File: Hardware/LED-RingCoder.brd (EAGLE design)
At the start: 40.6 x 40.6 mm, 37 parts, among them IC1 74LS595D, IC2 74LS595D, U1 ENCODER_RGB

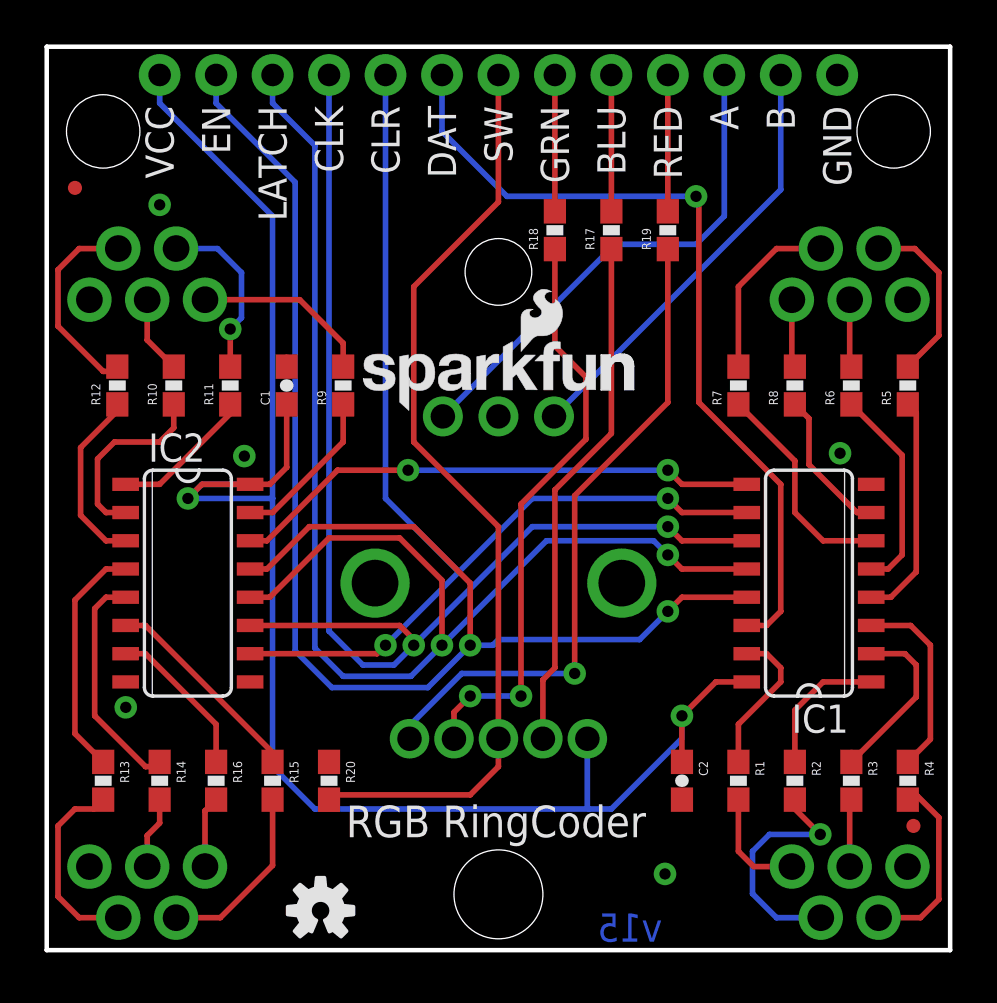
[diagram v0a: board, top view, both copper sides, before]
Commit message: Adding EN/GND and CLR/VCC jumpers
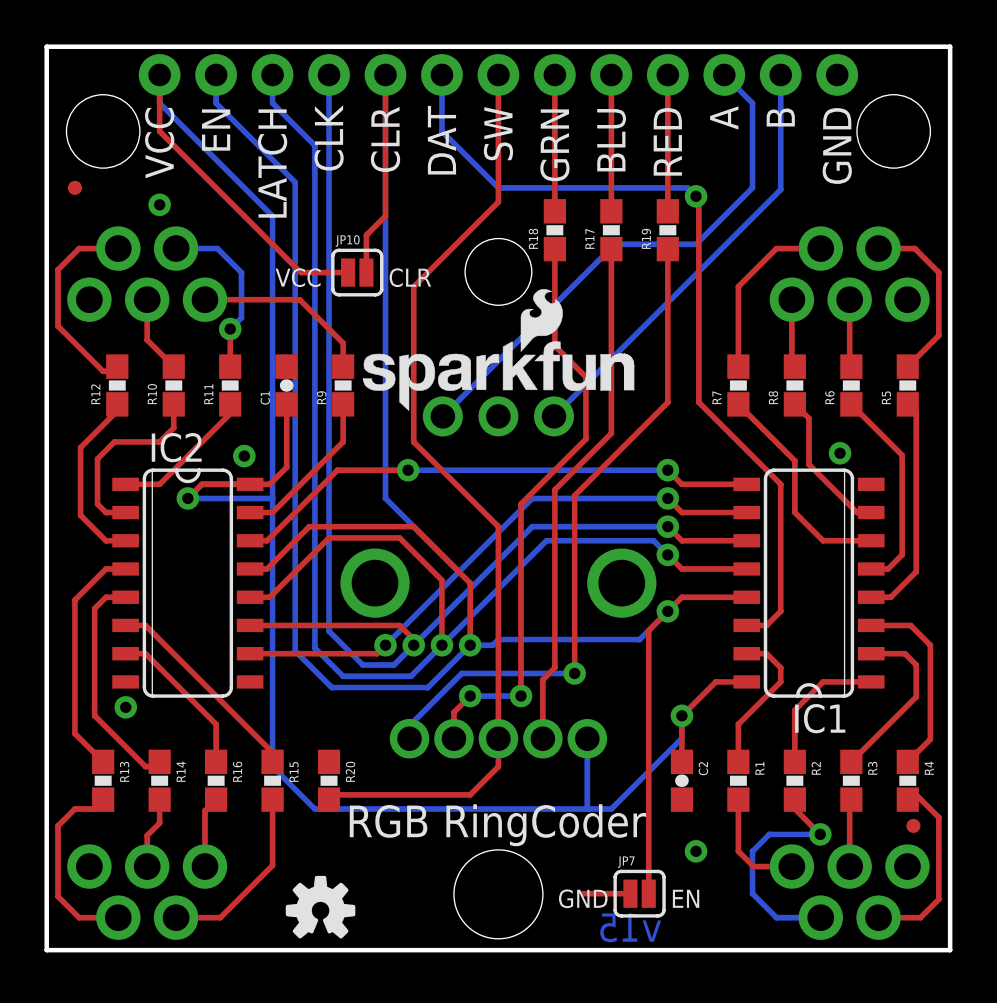
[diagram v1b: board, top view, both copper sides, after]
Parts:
- added JP10, JP7: (no value), SparkFun-Passives:SJ_2S
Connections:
- net CLEAR: now also JP10.2
- net EN: now also JP7.2
- net GND: now also JP7.1
- net VCC: now also JP10.1
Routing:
- net VCC: track 78.3 -> 91.9 mm
- net EN: track 64.6 -> 77.7 mm
- net CLEAR: track 49.2 -> 58.5 mm
- net GND: track 0.42 -> 2.55 mm
- net A: track 22.7 -> 23.8 mm

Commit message: Moving VCC/CLR jumper
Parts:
- moved JP10 27.9 mm to (14.0, 2.54), turned to 180 degrees
- moved U$2 19.0 mm to (31.4, 1.78)
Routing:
- net VCC: track 91.9 -> 84.1 mm, vias 2 -> 3
- net CLEAR: track 58.5 -> 60.9 mm, vias 2 -> 4
- net GND: vias 5 -> 6
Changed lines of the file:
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@@
 <text x="27.305" y="-10.16" size="1.778" layer="51" font="vector" ratio="15">Jim Lindblom</text>
 <text x="27.305" y="-13.335" size="1.778" layer="51" font="vector" ratio="15">Toni Klopfenstein</text>
-<text x="10.287" y="29.845" size="0.8128" layer="21" font="vector" ratio="20">VCC</text>
+<text x="15.367" y="1.905" size="0.8128" layer="21" font="vector" ratio="20">VCC</text>
 <text x="28.067" y="1.905" size="0.8128" layer="21" font="vector" ratio="20">EN</text>
-<text x="15.367" y="29.845" size="0.8128" layer="21" font="vector" ratio="20">CLR</text>
+<text x="10.287" y="1.905" size="0.8128" layer="21" font="vector" ratio="20">CLR</text>
 <text x="22.987" y="1.905" size="0.8128" layer="21" font="vector" ratio="20">GND</text>
 </plain>
@@
 <attribute name="VALUE" value="0.1uF" x="28.575" y="7.62" size="1.778" layer="27" rot="R270" display="off"/>
 </element>
-<element name="U$2" library="SparkFun" package="OSHW-LOGO-S" value="OSHW-LOGOS" x="12.319" y="1.778"/>
+<element name="U$2" library="SparkFun" package="OSHW-LOGO-S" value="OSHW-LOGOS" x="31.369" y="1.778"/>
 <element name="JP5" library="abes" package="FIDUCIAL-1X2.5" value="FIDUCIAL1X2.5" x="38.989" y="5.588"/>
 <element name="JP8" library="abes" package="FIDUCIAL-1X2.5" value="FIDUCIAL1X2.5" x="1.27" y="34.29"/>
@@
 <element name="U$1" library="SparkFun-Aesthetics" package="REVISION" value="REVISION" x="8.255" y="-12.7"/>
 <element name="JP7" library="SparkFun-Passives" package="SJ_2S" value="" x="26.67" y="2.54"/>
-<element name="JP10" library="SparkFun-Passives" package="SJ_2S" value="" x="13.97" y="30.48"/>
+<element name="JP10" library="SparkFun-Passives" package="SJ_2S" value="" x="13.97" y="2.54" rot="R180"/>
 </elements>
 <signals>
@@
 <contactref element="JP7" pad="1"/>
 <wire x1="26.2581" y1="2.54" x2="24.13" y2="2.54" width="0.254" layer="1"/>
+<via x="10.16" y="1.27" extent="1-16" drill="0.508"/>
 </signal>
 <signal name="4">
@@
 <contactref element="C1" pad="1"/>
 <contactref element="U1" pad="VCC"/>
-<wire x1="12.065" y1="6.35" x2="24.384" y2="6.35" width="0.254" layer="16"/>
 <wire x1="24.384" y1="6.35" x2="25.4" y2="6.35" width="0.254" layer="16"/>
 <wire x1="28.575" y1="10.541" x2="28.575" y2="8.47" width="0.254" layer="1"/>
@@
 <wire x1="25.4" y1="6.35" x2="28.575" y2="9.525" width="0.254" layer="16"/>
 <wire x1="28.575" y1="9.525" x2="28.575" y2="10.541" width="0.254" layer="16"/>
-<wire x1="31.49" y1="12.065" x2="30.099" y2="12.065" width="0.254" layer="1"/>
-<wire x1="30.099" y1="12.065" x2="28.575" y2="10.541" width="0.254" layer="1"/>
 <wire x1="5.08" y1="39.37" x2="5.08" y2="38.1" width="0.254" layer="16"/>
 <via x="6.35" y="20.32" extent="1-16" drill="0.508"/>
 <wire x1="9.15" y1="20.955" x2="6.985" y2="20.955" width="0.254" layer="1"/>
 <wire x1="6.985" y1="20.955" x2="6.35" y2="20.32" width="0.254" layer="1"/>
-<wire x1="9.15" y1="20.955" x2="6.985" y2="20.955" width="0.254" layer="16"/>
-<wire x1="6.985" y1="20.955" x2="6.35" y2="20.32" width="0.254" layer="16"/>
-<wire x1="12.065" y1="6.35" x2="10.16" y2="8.255" width="0.254" layer="16"/>
-<wire x1="10.16" y1="8.255" x2="10.16" y2="20.32" width="0.254" layer="16"/>
+<wire x1="10.16" y1="5.08" x2="10.16" y2="20.32" width="0.254" layer="16"/>
 <wire x1="10.16" y1="33.02" x2="10.16" y2="20.32" width="0.254" layer="16"/>
 <wire x1="10.16" y1="20.32" x2="6.35" y2="20.32" width="0.254" layer="16"/>
 <wire x1="10.16" y1="33.02" x2="5.08" y2="38.1" width="0.254" layer="16"/>
 <contactref element="JP10" pad="1"/>
-<wire x1="10.16" y1="31.75" x2="8.89" y2="33.02" width="0.254" layer="1"/>
-<wire x1="8.89" y1="33.02" x2="5.08" y2="36.83" width="0.254" layer="1"/>
-<wire x1="5.08" y1="36.83" x2="5.08" y2="39.37" width="0.254" layer="1"/>
-<wire x1="13.5581" y1="30.48" x2="11.43" y2="30.48" width="0.254" layer="1"/>
-<wire x1="11.43" y1="30.48" x2="10.16" y2="31.75" width="0.254" layer="1"/>
+<wire x1="31.49" y1="12.065" x2="30.099" y2="12.065" width="0.254" layer="1"/>
+<wire x1="30.099" y1="12.065" x2="28.575" y2="10.541" width="0.254" layer="1"/>
+<wire x1="24.32" y1="6.414" x2="19.114" y2="6.414" width="0.254" layer="16"/>
+<wire x1="17.78" y1="3.81" x2="16.002" y2="3.81" width="0.254" layer="16"/>
+<wire x1="16.002" y1="3.81" x2="11.43" y2="3.81" width="0.254" layer="16"/>
+<via x="15.875" y="4.699" extent="1-16" drill="0.508"/>
+<wire x1="19.114" y1="6.414" x2="19.114" y2="5.144" width="0.254" layer="16"/>
+<wire x1="19.114" y1="5.144" x2="17.78" y2="3.81" width="0.254" layer="16"/>
+<wire x1="10.16" y1="5.08" x2="11.43" y2="3.81" width="0.254" layer="16"/>
+<wire x1="15.875" y1="4.699" x2="15.875" y2="3.937" width="0.254" layer="16"/>
+<wire x1="15.875" y1="3.937" x2="16.002" y2="3.81" width="0.254" layer="16"/>
+<wire x1="14.3819" y1="2.54" x2="14.3819" y2="4.0949" width="0.254" layer="1"/>
+<wire x1="14.3819" y1="4.0949" x2="14.859" y2="4.572" width="0.254" layer="1"/>
+<wire x1="14.859" y1="4.572" x2="15.748" y2="4.572" width="0.254" layer="1"/>
+<wire x1="15.748" y1="4.572" x2="15.875" y2="4.699" width="0.254" layer="1"/>
 </signal>
 <signal name="QH*">
@@
 <wire x1="28.575" y1="19.685" x2="31.49" y2="19.685" width="0.254" layer="1"/>
 <wire x1="27.94" y1="20.32" x2="28.575" y2="19.685" width="0.254" layer="1"/>
-<wire x1="9.15" y1="13.335" x2="14.859" y2="13.335" width="0.254" layer="1"/>
+<wire x1="9.15" y1="13.335" x2="11.43" y2="13.335" width="0.254" layer="1"/>
+<wire x1="11.43" y1="13.335" x2="14.859" y2="13.335" width="0.254" layer="1"/>
 <wire x1="14.859" y1="13.335" x2="15.24" y2="13.716" width="0.254" layer="1"/>
 <wire x1="15.24" y1="13.716" x2="18.542" y2="17.018" width="0.254" layer="16"/>
@@
 <via x="15.24" y="13.716" extent="1-16" drill="0.508"/>
 <contactref element="JP10" pad="2"/>
-<wire x1="14.3819" y1="30.48" x2="14.3819" y2="32.1619" width="0.254" layer="1"/>
-<wire x1="14.3819" y1="32.1619" x2="15.24" y2="33.02" width="0.254" layer="1"/>
-<wire x1="15.24" y1="33.02" x2="15.24" y2="39.37" width="0.254" layer="1"/>
+<wire x1="13.5581" y1="2.54" x2="13.5581" y2="4.2219" width="0.254" layer="1"/>
+<wire x1="13.5581" y1="4.2219" x2="12.7" y2="5.08" width="0.254" layer="1"/>
+<via x="12.7" y="5.08" extent="1-16" drill="0.508"/>
+<wire x1="12.7" y1="5.08" x2="12.7" y2="10.16" width="0.254" layer="16"/>
+<wire x1="12.7" y1="10.16" x2="11.43" y2="11.43" width="0.254" layer="16"/>
+<via x="11.43" y="11.43" extent="1-16" drill="0.508"/>
+<wire x1="11.43" y1="11.43" x2="11.43" y2="13.335" width="0.254" layer="1"/>
 </signal>
 <signal name="EN">
